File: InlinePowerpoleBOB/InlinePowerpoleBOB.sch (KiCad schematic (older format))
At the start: 17 parts, among them IC1 LTC4368IMS-2#PBF, J1 Anderson_Powerpole_2w, J2 Anderson_Powerpole_2w, Q1 DMT6002LPS-13, Q2 DMT6002LPS-13

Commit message: PCB Updates
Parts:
- J1, J2: footprint SamacSys_Parts:Anderson_powerpole_2w -> SamacSys_Parts:Anderson_powerpole_2w_90
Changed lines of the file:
@@
 F 0 "J1" H 1813 3975 50  0000 C CNN
 F 1 "Anderson_Powerpole_2w" H 1813 3884 50  0000 C CNN
-F 2 "SamacSys_Parts:Anderson_powerpole_2w" H 1850 3750 50  0001 C CNN
+F 2 "SamacSys_Parts:Anderson_powerpole_2w_90" H 1850 3750 50  0001 C CNN
 F 3 "~" H 1850 3750 50  0001 C CNN
 	1    1850 3750
@@
 F 0 "J2" H 7669 3800 50  0000 L CNN
 F 1 "Anderson_Powerpole_2w" H 7669 3709 50  0000 L CNN
-F 2 "SamacSys_Parts:Anderson_powerpole_2w" H 7500 3800 50  0001 C CNN
+F 2 "SamacSys_Parts:Anderson_powerpole_2w_90" H 7500 3800 50  0001 C CNN
 F 3 "~" H 7500 3800 50  0001 C CNN
 	1    7500 3800

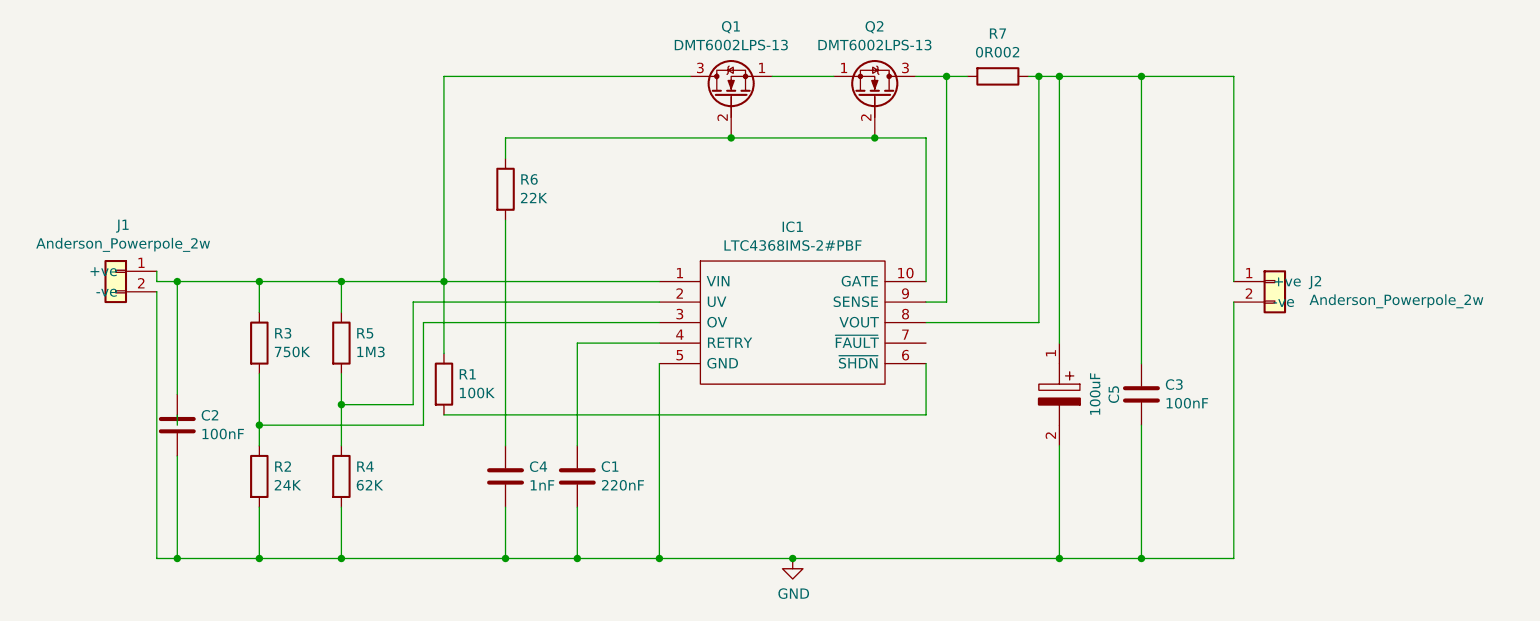
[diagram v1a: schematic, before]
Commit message: Removed over current feature
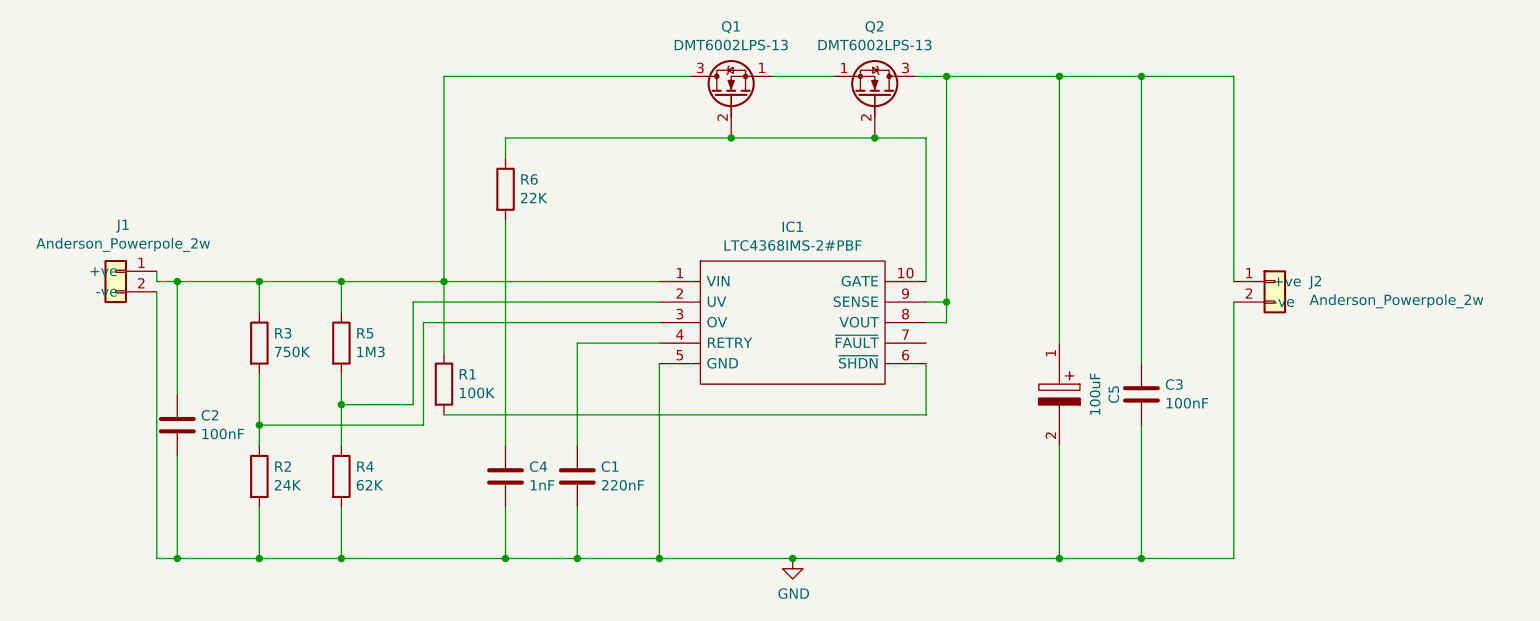
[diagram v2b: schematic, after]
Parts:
- removed R7: 0R002, Resistor_SMD:R_2512_6332Metric_Pad1.40x3.35mm_HandSolder, symbol Device:R
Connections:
- wire segments 67 -> 64
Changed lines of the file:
@@
 Wire Wire Line
 	6450 4100 6450 2800
-$Comp
-L Device:R R7
-U 1 1 61214CA0
-P 6150 2800
-F 0 "R7" V 5943 2800 50  0000 C CNN
-F 1 "0R002" V 6034 2800 50  0000 C CNN
-F 2 "Resistor_SMD:R_2512_6332Metric_Pad1.40x3.35mm_HandSolder" V 6080 2800 50  0001 C CNN
-F 3 "~" H 6150 2800 50  0001 C CNN
-	1    6150 2800
-	0    1    1    0
-$EndComp
 Wire Wire Line
 	3450 4450 5800 4450
@@
 Wire Wire Line
 	4100 4100 4500 4100
-Wire Wire Line
-	6000 2800 5900 2800
-Connection ~ 5900 2800
-Wire Wire Line
-	6300 2800 6350 2800
-Wire Wire Line
-	5800 4000 6350 4000
-Wire Wire Line
-	6350 4000 6350 2800
-Connection ~ 6350 2800
-Wire Wire Line
-	6350 2800 6450 2800
 Connection ~ 5150 5150
 Wire Wire Line
@@
 Wire Wire Line
 	7300 2800 7300 3800
-Connection ~ 6450 2800
 Wire Wire Line
 	6850 4200 6850 2800
@@
 	6850 2800 7300 2800
 Wire Wire Line
-	2150 4450 2150 4500
+	5900 2800 6450 2800
+Connection ~ 5900 2800
+Connection ~ 6450 2800
+Wire Wire Line
+	5800 4000 5900 4000
+Wire Wire Line
+	5900 4000 5900 3900
+Connection ~ 5900 3900
 $EndSCHEMATC

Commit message: V1.1 update
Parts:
- removed R2: 24K, Resistor_SMD:R_0805_2012Metric_Pad1.20x1.40mm_HandSolder, symbol Device:R
- added D1: 15V, Diode_SMD:D_0805_2012Metric, symbol Device:D_Zener
- R2: renamed from R4; value 62K -> 24K
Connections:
- net GND: now also D1.2 (A)
- net at IC1.2 (UV), R5.2: now also D1.1 (K); no longer R2.1
- net at IC1.3 (OV), R3.2: now also R2.1
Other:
- moved on the sheet: R2
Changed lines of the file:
@@
 Wire Wire Line
 	5800 4450 5800 4200
-$Comp
-L Device:R R2
-U 1 1 611EDEB5
-P 2550 4750
-F 0 "R2" H 2620 4796 50  0000 L CNN
-F 1 "24K" H 2620 4705 50  0000 L CNN
-F 2 "Resistor_SMD:R_0805_2012Metric_Pad1.20x1.40mm_HandSolder" V 2480 4750 50  0001 C CNN
-F 3 "~" H 2550 4750 50  0001 C CNN
-	1    2550 4750
-	1    0    0    -1
-$EndComp
 Wire Wire Line
 	2550 4900 2550 5150
@@
 	2950 4900 2950 5150
 $Comp
-L Device:R R4
+L Device:R R2
 U 1 1 611F020F
-P 2950 4750
-F 0 "R4" H 3020 4796 50  0000 L CNN
-F 1 "62K" H 3020 4705 50  0000 L CNN
-F 2 "Resistor_SMD:R_0805_2012Metric_Pad1.20x1.40mm_HandSolder" V 2880 4750 50  0001 C CNN
-F 3 "~" H 2950 4750 50  0001 C CNN
-	1    2950 4750
+P 2550 4750
+F 0 "R2" H 2620 4796 50  0000 L CNN
+F 1 "24K" H 2620 4705 50  0000 L CNN
+F 2 "Resistor_SMD:R_0805_2012Metric_Pad1.20x1.40mm_HandSolder" V 2480 4750 50  0001 C CNN
+F 3 "~" H 2550 4750 50  0001 C CNN
+	1    2550 4750
 	1    0    0    -1
 $EndComp
@@
 Wire Wire Line
 	2950 5150 3750 5150
-Wire Wire Line
-	2950 5150 2550 5150
 Connection ~ 2950 5150
-Wire Wire Line
-	2550 5150 2150 5150
-Connection ~ 2550 5150
 Connection ~ 2150 5150
 Connection ~ 4100 5150
@@
 	5900 4000 5900 3900
 Connection ~ 5900 3900
+$Comp
+L Device:D_Zener D1
+U 1 1 6165A556
+P 2950 4750
+F 0 "D1" V 2904 4830 50  0000 L CNN
+F 1 "15V" V 2995 4830 50  0000 L CNN
+F 2 "Diode_SMD:D_0805_2012Metric" H 2950 4750 50  0001 C CNN
+F 3 "~" H 2950 4750 50  0001 C CNN
+	1    2950 4750
+	0    1    1    0
+$EndComp
+Wire Wire Line
+	2150 5150 2550 5150
+Connection ~ 2550 5150
+Wire Wire Line
+	2550 5150 2950 5150
 $EndSCHEMATC
